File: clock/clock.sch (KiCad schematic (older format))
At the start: 46 parts, among them J1 Conn_01x16_Male, J2 Conn_01x16_Male, J3 Conn_01x01_Male, J4 Conn_01x01_Male, J5 Conn_01x01_Male, J6 Conn_01x01_Male, U1 iv12, U2 iv12, U3 iv12, U4 iv12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

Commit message: Clock rev 2 with controller
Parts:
- removed J1, J2: Conn_01x16_Male, Connector_PinHeader_2.54mm:PinHeader_1x16_P2.54mm_Vertical, symbol Connector:Conn_01x16_Male
- removed J3, J4, J5, J6: Conn_01x01_Male, Connector_PinHeader_2.54mm:PinHeader_1x01_P2.54mm_Vertical, symbol Connector:Conn_01x01_Male
- added BT1: 3v, Battery:BatteryHolder_Keystone_3000_1x12mm, symbol Device:Battery_Cell
- added C1, C2: 10u, Capacitor_SMD:C_1206_3216Metric_Pad1.42x1.75mm_HandSolder, symbol Device:C_Small
- added C3, C4, C5, C6: .1u, Capacitor_SMD:C_0603_1608Metric_Pad1.05x0.95mm_HandSolder, symbol Device:C_Small
- added D1, D2, D3, D4: LED_Small, LED_SMD:LED_0805_2012Metric_Pad1.15x1.40mm_HandSolder, symbol Device:LED_Small
- added D5: D_Schottky, Diode_SMD:D_SMA, symbol Device:D_Schottky
- added J1: USB_OTG-conn1, Connector_USB:USB_Micro-B_Molex-105133-0001, symbol clock-rescue:USB_OTG-conn1
- added L1: L_Small, Inductor_SMD:L_10.4x10.4_H4.8, symbol Device:L_Small
- added R33, R34, R35, R36: 470, Resistor_SMD:R_0603_1608Metric_Pad1.05x0.95mm_HandSolder, symbol Device:R_Small
- added R37: 82k, Resistor_SMD:R_0603_1608Metric_Pad1.05x0.95mm_HandSolder, symbol Device:R_Small
- added R38: 2.2k, Resistor_SMD:R_0603_1608Metric_Pad1.05x0.95mm_HandSolder, symbol Device:R_Small
- added R39, R40: 10k, Resistor_SMD:R_0603_1608Metric_Pad1.05x0.95mm_HandSolder, symbol Device:R_Small
- added R41, R42: 22, Resistor_SMD:R_0603_1608Metric_Pad1.05x0.95mm_HandSolder, symbol Device:R_Small
- added SW1, SW2, SW3, SW4, SW5: SW_SPST, Button_Switch_SMD:SW_SPST_TL3342, symbol Switch:SW_SPST
- added U10, U9: PCA9685PW, Package_SO:TSSOP-28_4.4x9.7mm_P0.65mm, symbol Driver_LED:PCA9685PW
- added U11: ATmega32U2-AU, Package_QFP:TQFP-32_7x7mm_P0.8mm, symbol MCU_Microchip_ATmega:ATmega32U2-AU
- added U12: DS3231M, Package_SO:SOIC-16W_7.5x10.3mm_P1.27mm, symbol Timer_RTC:DS3231M
- added U13: MT3608, Package_TO_SOT_SMD:SOT-23-6_Handsoldering, symbol iv12:MT3608
- renumbered U2 to U1, U1 to U2, U6 to U5, U5 to U6
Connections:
- net labels added: DOWN, MODE, OTHER, RST, SCL, SDA, UP
- wire segments 272 -> 416
- no-connect marks 0 -> 3
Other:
- moved on the sheet: R1, R10, R11, R12, R13, R14, R15, R16, R17, R18, R19, R2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

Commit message: Rev 3 pcb
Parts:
- removed U11: ATmega32U2-AU, Package_QFP:TQFP-32_7x7mm_P0.8mm, symbol MCU_Microchip_ATmega:ATmega32U2-AU
- added C7, C8: 22p, Capacitor_SMD:C_0603_1608Metric_Pad1.05x0.95mm_HandSolder, symbol Device:C_Small
- added C9: .1u, Capacitor_SMD:C_0603_1608Metric_Pad1.05x0.95mm_HandSolder, symbol Device:C_Small
- added R43: 10k, Resistor_SMD:R_0603_1608Metric_Pad1.05x0.95mm_HandSolder, symbol Device:R_Small
- added TP1, TP2, TP3, TP4, TP5: TestPoint, TestPoint:TestPoint_Plated_Hole_D2.0mm, symbol Connector:TestPoint
- added U11: ATmega32U4-AU, Package_DFN_QFN:QFN-44-1EP_7x7mm_P0.5mm_EP5.15x5.15mm, symbol MCU_Microchip_ATmega:ATmega32U4-AU
- added Y1: 16Mhz, Crystal:Crystal_SMD_5032-4Pin_5.0x3.2mm, symbol Device:Crystal_GND24
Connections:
- wire segments 416 -> 447
- no-connect marks 3 -> 5
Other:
- moved on the sheet: J1, R39, R40, R41, R42

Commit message: Rev 4 PCB
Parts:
- removed C5, C9: .1u, Capacitor_SMD:C_0603_1608Metric_Pad1.05x0.95mm_HandSolder, symbol Device:C_Small
- removed C7, C8: 22p, Capacitor_SMD:C_0603_1608Metric_Pad1.05x0.95mm_HandSolder, symbol Device:C_Small
- removed J1: USB_OTG-conn1, Connector_USB:USB_Micro-B_Molex-105133-0001, symbol clock-rescue:USB_OTG-conn1
- removed R41, R42: 22, Resistor_SMD:R_0603_1608Metric_Pad1.05x0.95mm_HandSolder, symbol Device:R_Small
- removed TP1, TP2, TP3, TP4, TP5: TestPoint, TestPoint:TestPoint_Plated_Hole_D2.0mm, symbol Connector:TestPoint
- removed U11: ATmega32U4-AU, Package_DFN_QFN:QFN-44-1EP_7x7mm_P0.5mm_EP5.15x5.15mm, symbol MCU_Microchip_ATmega:ATmega32U4-AU
- removed Y1: 16Mhz, Crystal:Crystal_SMD_5032-4Pin_5.0x3.2mm, symbol Device:Crystal_GND24
- added J1: FTDI, Connector_PinHeader_2.54mm:PinHeader_1x06_P2.54mm_Vertical, symbol Connector:Conn_01x06_Female
- added J2: USB, Connector_USB:USB_Micro-B_Molex-105133-0001, symbol clock-rescue:USB_OTG-conn1
- added J3: TP, Connector_PinHeader_2.54mm:PinHeader_1x05_P2.54mm_Vertical, symbol Connector:Conn_01x05_Female
- added U11: ATmega328P-AU, Package_QFP:TQFP-32_7x7mm_P0.8mm, symbol MCU_Microchip_ATmega:ATmega328P-AU
- added Y1: 16MHz, Crystal:Resonator_SMD_muRata_CSTxExxV-3Pin_3.0x1.1mm_HandSoldering, symbol Device:Crystal_GND3
- L1: value L_Small -> 22 uH
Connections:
- net +24V: now also J3.3 (Pin_3)
- net +5V: now also J2.1 (VBUS), J3.2 (Pin_2), U11.18 (AVCC), U11.4 (VCC), U11.6 (VCC)
- net DOWN: now also U11.13 (PB1)
- net GND: now also J1.1 (Pin_1), J2.4 (ID), J2.5 (GND), J2.6 (Shield), J3.1 (Pin_1), U11.21 (GND), U11.3 (GND), U11.5 (GND), Y1.3
- net MODE: now also U11.14 (PB2)
- net OTHER: now also U11.15 (PB3)
- net RST: now also J1.6 (Pin_6), U11.29 (~RESET~/PC6)
- net SCL: now also J3.4 (Pin_4), U11.28 (PC5)
- net SDA: now also J3.5 (Pin_5), U11.27 (PC4)
- net UP: now also U11.12 (PB0)
- new net: U11.7 (XTAL1/PB6), Y1.1
- new net: U11.8 (XTAL2/PB7), Y1.2
- new net CTS: J1.2 (Pin_2)
- new net RX: J1.4 (Pin_4), U11.30 (PD0)
- new net TX: J1.5 (Pin_5), U11.31 (PD1)
- no-connect marks 5 -> 3
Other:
- moved on the sheet: R39, R40, R43

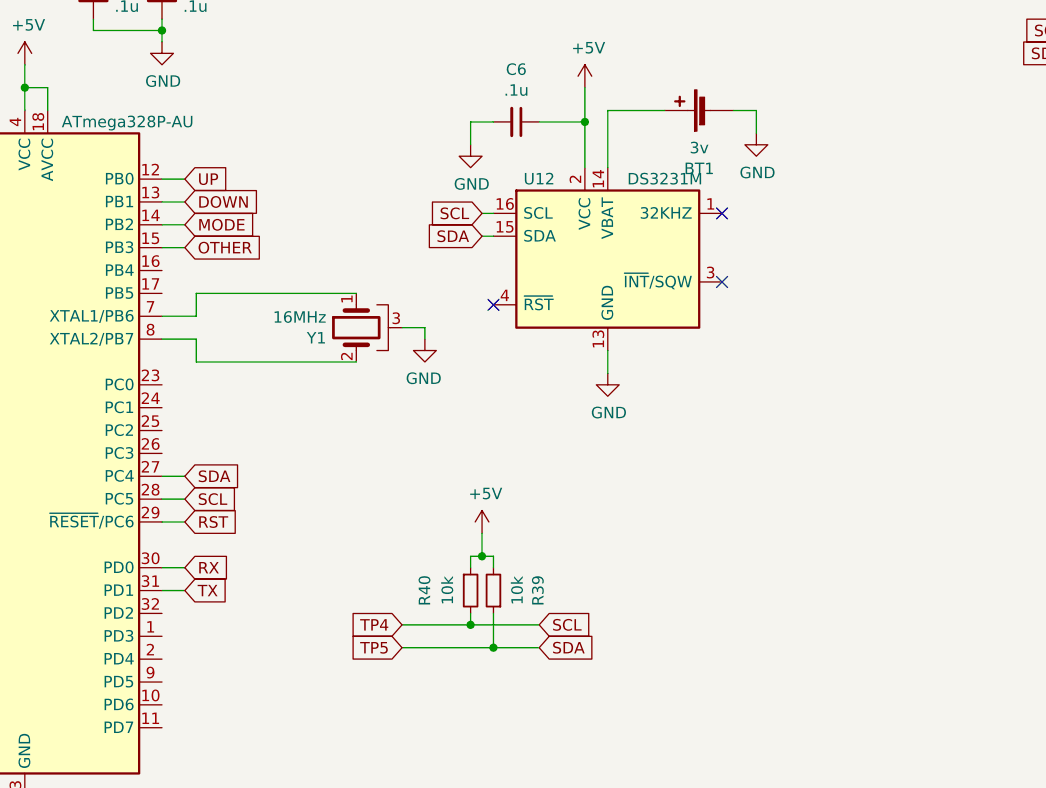
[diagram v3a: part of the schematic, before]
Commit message: Hooked up SQW from RTC to MCU
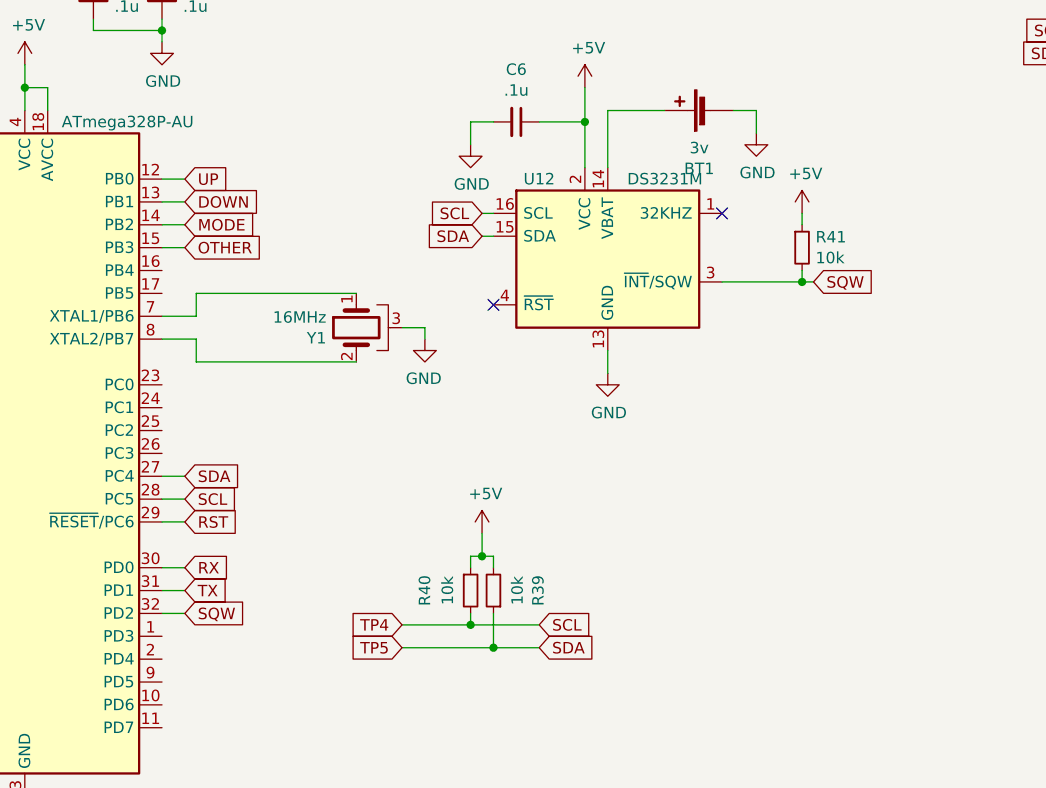
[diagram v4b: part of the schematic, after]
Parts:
- added R41: 10k, Resistor_SMD:R_0603_1608Metric_Pad1.05x0.95mm_HandSolder, symbol clock-rescue:R_Small-device1
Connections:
- net +5V: now also R41.1
- net SQW: now reaches U11.32 (PD2)
- net SQW: now also U12.3 (~INT~/SQW), R41.2
- no-connect marks 3 -> 2
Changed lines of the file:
@@
 Wire Wire Line
 	11700 8350 11700 8450
-$Comp
-L Timer_RTC:DS3231M U12
-U 1 1 5C88E5FC
-P 8100 3400
-F 0 "U12" H 7800 3750 50  0000 C CNN
-F 1 "DS3231M" H 8350 3750 50  0000 C CNN
-F 2 "Package_SO:SOIC-16W_7.5x10.3mm_P1.27mm" H 8100 2800 50  0001 C CNN
-F 3 "http://datasheets.maximintegrated.com/en/ds/DS3231.pdf" H 8370 3450 50  0001 C CNN
-	1    8100 3400
-	1    0    0    -1
-$EndComp
 Text GLabel 7550 3200 0    50   Input ~ 0
 SCL
@@
 $EndComp
 NoConn ~ 8600 3200
-NoConn ~ 8600 3500
 Wire Wire Line
 	8100 3000 8100 2750
@@
 Wire Wire Line
 	3500 5250 4000 5250
+$Comp
+L Timer_RTC:DS3231M U12
+U 1 1 5C88E5FC
+P 8100 3400
+F 0 "U12" H 7800 3750 50  0000 C CNN
+F 1 "DS3231M" H 8350 3750 50  0000 C CNN
+F 2 "Package_SO:SOIC-16W_7.5x10.3mm_P1.27mm" H 8100 2800 50  0001 C CNN
+F 3 "http://datasheets.maximintegrated.com/en/ds/DS3231.pdf" H 8370 3450 50  0001 C CNN
+	1    8100 3400
+	1    0    0    -1
+$EndComp
+Text GLabel 9000 3500 2    50   Input ~ 0
+SQW
+Text GLabel 6250 4950 2    50   Input ~ 0
+SQW
+Wire Wire Line
+	6250 4950 6150 4950
+$Comp
+L clock-rescue:R_Small-device1 R41
+U 1 1 5C7F1BCB
+P 8950 3350
+F 0 "R41" H 9009 3396 50  0000 L CNN
+F 1 "10k" H 9009 3305 50  0000 L CNN
+F 2 "Resistor_SMD:R_0603_1608Metric_Pad1.05x0.95mm_HandSolder" H 8950 3350 50  0001 C CNN
+F 3 "" H 8950 3350 50  0001 C CNN
+	1    8950 3350
+	1    0    0    -1
+$EndComp
+$Comp
+L power:+5V #PWR0151
+U 1 1 5C7F27BA
+P 8950 3200
+F 0 "#PWR0151" H 8950 3050 50  0001 C CNN
+F 1 "+5V" H 8965 3373 50  0000 C CNN
+F 2 "" H 8950 3200 50  0001 C CNN
+F 3 "" H 8950 3200 50  0001 C CNN
+	1    8950 3200
+	1    0    0    -1
+$EndComp
+Wire Wire Line
+	8600 3500 8950 3500
+Wire Wire Line
+	8950 3450 8950 3500
+Connection ~ 8950 3500
+Wire Wire Line
+	8950 3500 9000 3500
+Wire Wire Line
+	8950 3200 8950 3250
 $EndSCHEMATC

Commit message: More cleanup
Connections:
- no-connect marks 2 -> 4
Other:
- moved on the sheet: J2
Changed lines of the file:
@@
 L power:+5V #PWR0134
 U 1 1 5D8C47A1
-P 3550 8450
-F 0 "#PWR0134" H 3550 8300 50  0001 C CNN
-F 1 "+5V" H 3565 8623 50  0000 C CNN
-F 2 "" H 3550 8450 50  0001 C CNN
-F 3 "" H 3550 8450 50  0001 C CNN
-	1    3550 8450
+P 3700 8450
+F 0 "#PWR0134" H 3700 8300 50  0001 C CNN
+F 1 "+5V" H 3715 8623 50  0000 C CNN
+F 2 "" H 3700 8450 50  0001 C CNN
+F 3 "" H 3700 8450 50  0001 C CNN
+	1    3700 8450
 	1    0    0    -1
 $EndComp
@@
 	7200 5000 7500 5000
 Wire Wire Line
-	3550 8450 3550 8550
-Wire Wire Line
-	3550 8550 3900 8550
+	3550 8550 3700 8550
 Wire Wire Line
 	7500 5000 7800 5000
@@
 	6250 4850 6150 4850
 $Comp
-L power:GND #PWR0147
-U 1 1 5CD38EBC
-P 2250 8350
-F 0 "#PWR0147" H 2250 8100 50  0001 C CNN
-F 1 "GND" H 2255 8177 50  0000 C CNN
-F 2 "" H 2250 8350 50  0001 C CNN
-F 3 "" H 2250 8350 50  0001 C CNN
-	1    2250 8350
-	1    0    0    -1
-$EndComp
-$Comp
-L power:+5V #PWR0148
-U 1 1 5CD75A01
-P 2800 7500
-F 0 "#PWR0148" H 2800 7350 50  0001 C CNN
-F 1 "+5V" H 2815 7673 50  0000 C CNN
-F 2 "" H 2800 7500 50  0001 C CNN
-F 3 "" H 2800 7500 50  0001 C CNN
-	1    2800 7500
-	1    0    0    -1
-$EndComp
-$Comp
 L clock-rescue:USB_OTG-conn1 J2
 U 1 1 5C6DC8AA
-P 2350 7800
-F 0 "J2" H 2407 8267 50  0000 C CNN
-F 1 "USB" H 2407 8176 50  0000 C CNN
-F 2 "Connector_USB:USB_Micro-B_Molex-105133-0001" H 2500 7750 50  0001 C CNN
-F 3 "" H 2500 7750 50  0001 C CNN
-	1    2350 7800
-	1    0    0    -1
-$EndComp
-Wire Wire Line
-	2650 7600 2800 7600
-Wire Wire Line
-	2800 7600 2800 7500
-Wire Wire Line
-	2250 8200 2250 8250
-Wire Wire Line
-	2250 8250 2350 8250
-Wire Wire Line
-	2350 8250 2350 8200
-Connection ~ 2250 8250
-Wire Wire Line
-	2250 8250 2250 8350
-Wire Wire Line
-	2350 8250 2700 8250
-Wire Wire Line
-	2700 8250 2700 8000
-Wire Wire Line
-	2700 8000 2650 8000
-Connection ~ 2350 8250
+P 3250 8750
+F 0 "J2" H 3307 9217 50  0000 C CNN
+F 1 "USB" H 3307 9126 50  0000 C CNN
+F 2 "Connector_USB:USB_Micro-B_Molex-105133-0001" H 3400 8700 50  0001 C CNN
+F 3 "" H 3400 8700 50  0001 C CNN
+	1    3250 8750
+	1    0    0    -1
+$EndComp
 $Comp
 L Connector:Conn_01x05_Female J3
@@
 Wire Wire Line
 	8950 3200 8950 3250
+Wire Wire Line
+	3150 9150 3150 9200
+Wire Wire Line
+	3150 9550 3900 9550
+Connection ~ 3900 9550
+Wire Wire Line
+	3250 9150 3250 9200
+Wire Wire Line
+	3250 9200 3150 9200
+Connection ~ 3150 9200
+Wire Wire Line
+	3150 9200 3150 9550
+Wire Wire Line
+	3250 9200 3600 9200
+Wire Wire Line
+	3600 9200 3600 8950
+Wire Wire Line
+	3600 8950 3550 8950
+Connection ~ 3250 9200
+NoConn ~ 3550 8750
+NoConn ~ 3550 8850
+Wire Wire Line
+	3700 8450 3700 8550
+Connection ~ 3700 8550
+Wire Wire Line
+	3700 8550 3900 8550
 $EndSCHEMATC

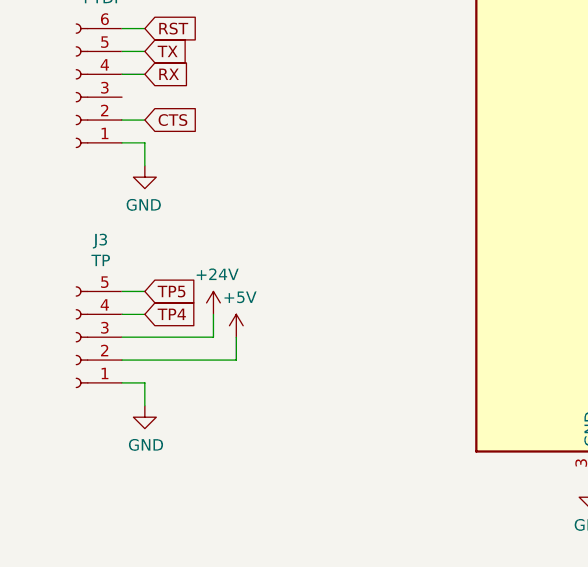
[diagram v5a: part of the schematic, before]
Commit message: Moved 24v test point
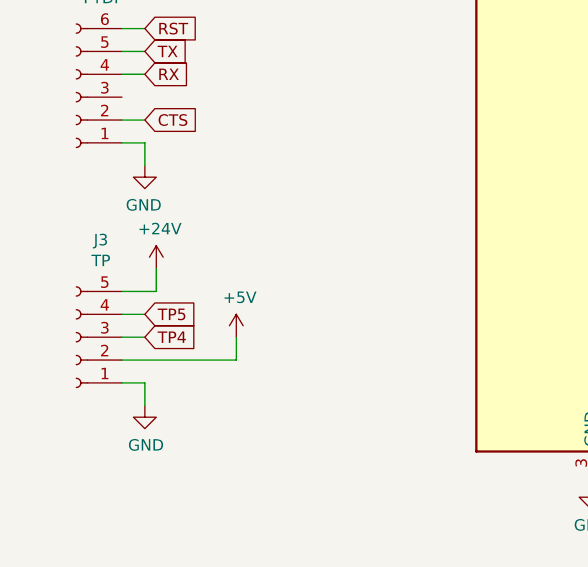
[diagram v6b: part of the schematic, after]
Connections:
- net +24V: now also J3.5 (Pin_5); no longer J3.3 (Pin_3)
- net SCL: now also J3.3 (Pin_3); no longer J3.4 (Pin_4)
- net SDA: now also J3.4 (Pin_4); no longer J3.5 (Pin_5)
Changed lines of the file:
@@
 Text GLabel 7200 5000 0    50   Input ~ 0
 TP4
-Text GLabel 3600 4950 2    50   Input ~ 0
+Text GLabel 3600 5050 2    50   Input ~ 0
 TP5
-Text GLabel 3600 5050 2    50   Input ~ 0
+Text GLabel 3600 5150 2    50   Input ~ 0
 TP4
 Wire Wire Line
@@
 Wire Wire Line
 	3500 5050 3600 5050
-Wire Wire Line
-	3600 4950 3500 4950
 $Comp
 L power:GND #PWR0140
@@
 L power:+24V #PWR0150
 U 1 1 5CA60D9F
-P 3900 5050
-F 0 "#PWR0150" H 3900 4900 50  0001 C CNN
-F 1 "+24V" H 3915 5223 50  0000 C CNN
-F 2 "" H 3900 5050 50  0001 C CNN
-F 3 "" H 3900 5050 50  0001 C CNN
-	1    3900 5050
+P 3650 4850
+F 0 "#PWR0150" H 3650 4700 50  0001 C CNN
+F 1 "+24V" H 3665 5023 50  0000 C CNN
+F 2 "" H 3650 4850 50  0001 C CNN
+F 3 "" H 3650 4850 50  0001 C CNN
+	1    3650 4850
 	1    0    0    -1
 $EndComp
-Wire Wire Line
-	3900 5150 3900 5050
-Wire Wire Line
-	3500 5150 3900 5150
 Wire Wire Line
 	4000 5250 4000 5150
@@
 Wire Wire Line
 	3700 8550 3900 8550
+Wire Wire Line
+	3600 5150 3500 5150
+Wire Wire Line
+	3650 4850 3650 4950
+Wire Wire Line
+	3500 4950 3650 4950
 $EndSCHEMATC

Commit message: Clean up
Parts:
- BT1: value 3v -> CR1220
- R29, R30, R31, R32: value R_Small -> 27
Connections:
- net SCL: now also R39.1; no longer R40.2
- net SDA: now also R40.2; no longer R39.1
- no-connect marks 4 -> 5
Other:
- moved on the sheet: BT1, C1, C2, C6, D5, J1, J2, J3, L1, R37, R38, R39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

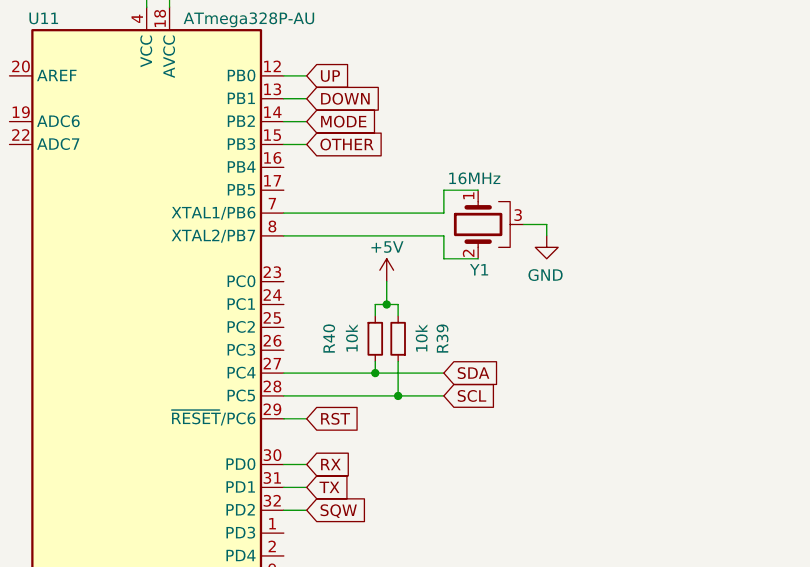
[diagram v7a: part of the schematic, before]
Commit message: Fixed crystal pinout
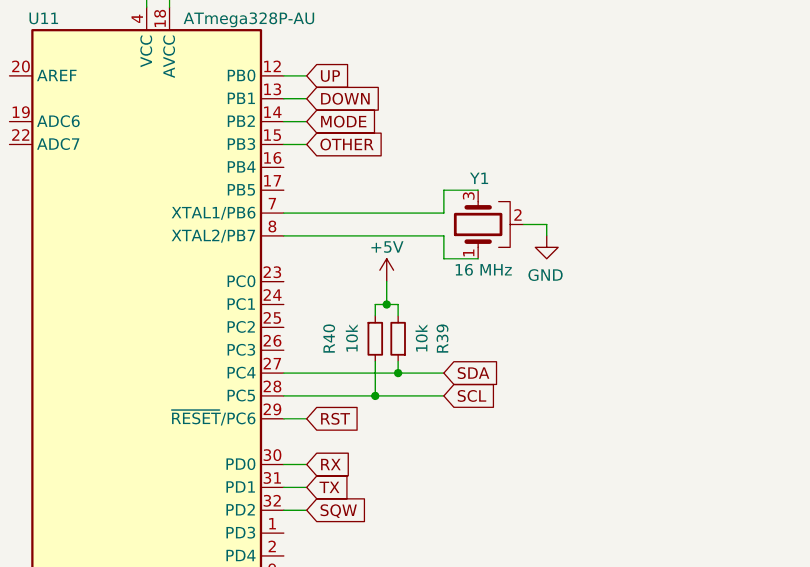
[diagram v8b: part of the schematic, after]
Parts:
- removed Y1: 16MHz, Crystal:Resonator_SMD_muRata_CSTxExxV-3Pin_3.0x1.1mm_HandSoldering, symbol Device:Crystal_GND3
- added Y1: 16 MHz, Crystal:Resonator_SMD_muRata_CSTxExxV-3Pin_3.0x1.1mm_HandSoldering, symbol Device:Crystal_GND2
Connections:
- net GND: now also Y1.2
- net SCL: now also R40.2; no longer R39.1
- net SDA: now also R39.1; no longer R40.2
- net at U11.7 (XTAL1/PB6): now also Y1.3
- net at U11.8 (XTAL2/PB7): now also Y1.1
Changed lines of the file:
@@
 	6550 4050 6600 4050
-Wire Wire Line
-	6550 4300 6550 4350
-Connection ~ 6550 4350
 Wire Wire Line
 	6600 3950 6600 4050
@@
 Wire Wire Line
 	1400 9500 1550 9500
-Wire Wire Line
-	6550 4350 6850 4350
-Wire Wire Line
-	6650 4300 6650 4450
-Connection ~ 6650 4450
-Wire Wire Line
-	6650 4450 6850 4450
 $Comp
 L MCU_Microchip_ATmega:ATmega328P-AU U11
@@
 Wire Wire Line
 	6250 4550 6150 4550
-$Comp
-L Device:Crystal_GND3 Y1
-U 1 1 5C910D8A
-P 7000 3700
-F 0 "Y1" V 7200 3650 50  0000 L CNN
-F 1 "16MHz" V 6800 3600 50  0000 L CNN
-F 2 "Crystal:Resonator_SMD_muRata_CSTxExxV-3Pin_3.0x1.1mm_HandSoldering" H 7000 3700 50  0001 C CNN
-F 3 "~" H 7000 3700 50  0001 C CNN
-	1    7000 3700
-	0    -1   1    0
-$EndComp
 $Comp
 L Connector:Conn_01x06_Female J1
@@
 NoConn ~ 1650 4400
 Wire Wire Line
-	6150 4450 6650 4450
-Wire Wire Line
-	6150 4350 6550 4350
-Wire Wire Line
 	6850 3750 6850 3850
 Wire Wire Line
@@
 Wire Wire Line
 	5550 2650 5650 2650
+Wire Wire Line
+	6150 4350 6650 4350
+Wire Wire Line
+	6150 4450 6550 4450
+Wire Wire Line
+	6550 4300 6550 4450
+Connection ~ 6550 4450
+Wire Wire Line
+	6550 4450 6850 4450
+Wire Wire Line
+	6650 4300 6650 4350
+Connection ~ 6650 4350
+Wire Wire Line
+	6650 4350 6850 4350
+$Comp
+L Device:Crystal_GND2 Y1
+U 1 1 5C9AFC31
+P 7000 3700
+F 0 "Y1" V 7200 3650 50  0000 L CNN
+F 1 "16 MHz" V 6800 3550 50  0000 L CNN
+F 2 "Crystal:Resonator_SMD_muRata_CSTxExxV-3Pin_3.0x1.1mm_HandSoldering" H 7000 3700 50  0001 C CNN
+F 3 "~" H 7000 3700 50  0001 C CNN
+	1    7000 3700
+	0    -1   -1   0
+$EndComp
 $EndSCHEMATC
